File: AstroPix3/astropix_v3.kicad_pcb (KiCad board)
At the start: 4 copper layers, 51.3 x 48.9 mm, 50 parts, among them J1 pcie_GECCO, J10 SPI_right, J2 ChipRings, J3 TempSens, J4 SFOut, J5 sample_clock_out, J6 HV_in_external, J7 Conn_01x03, J9 SPI_left, U2 SN65LVDS4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

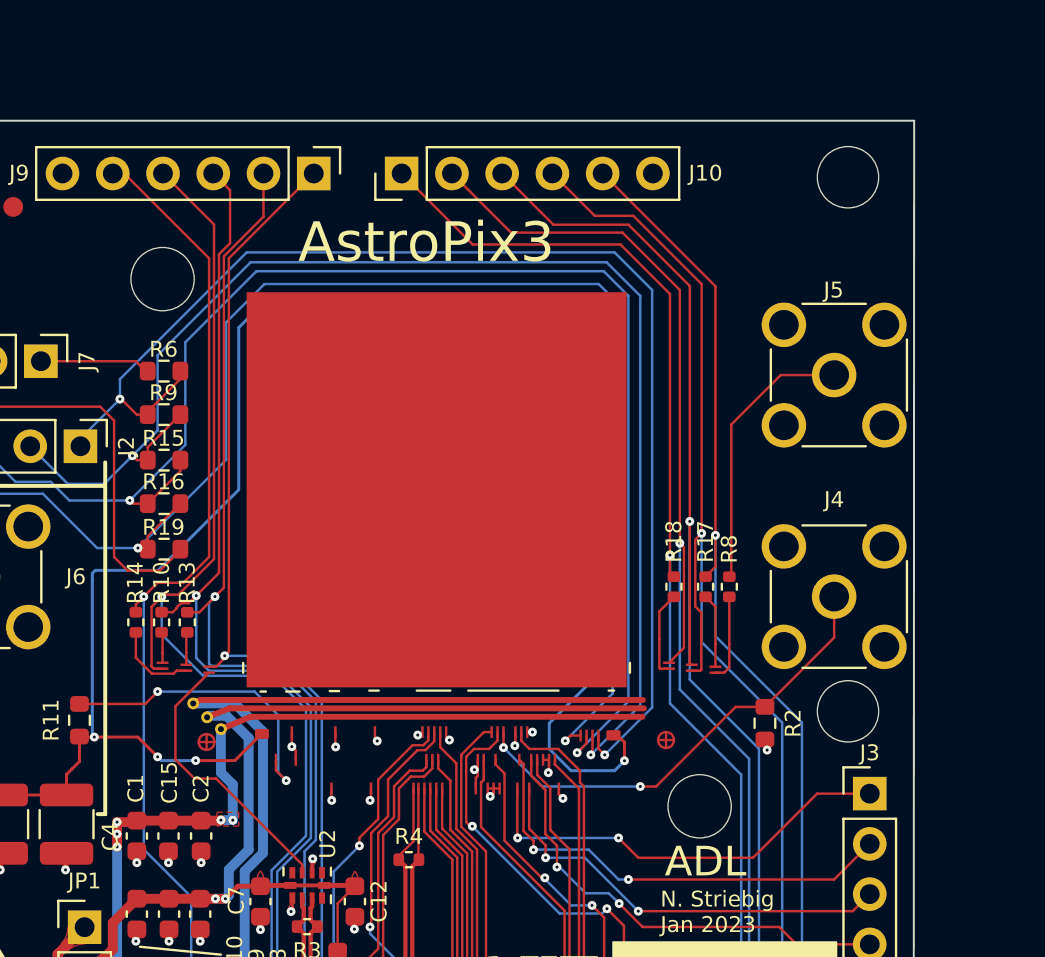
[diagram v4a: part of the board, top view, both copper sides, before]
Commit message: PCB: Connected HV Pad
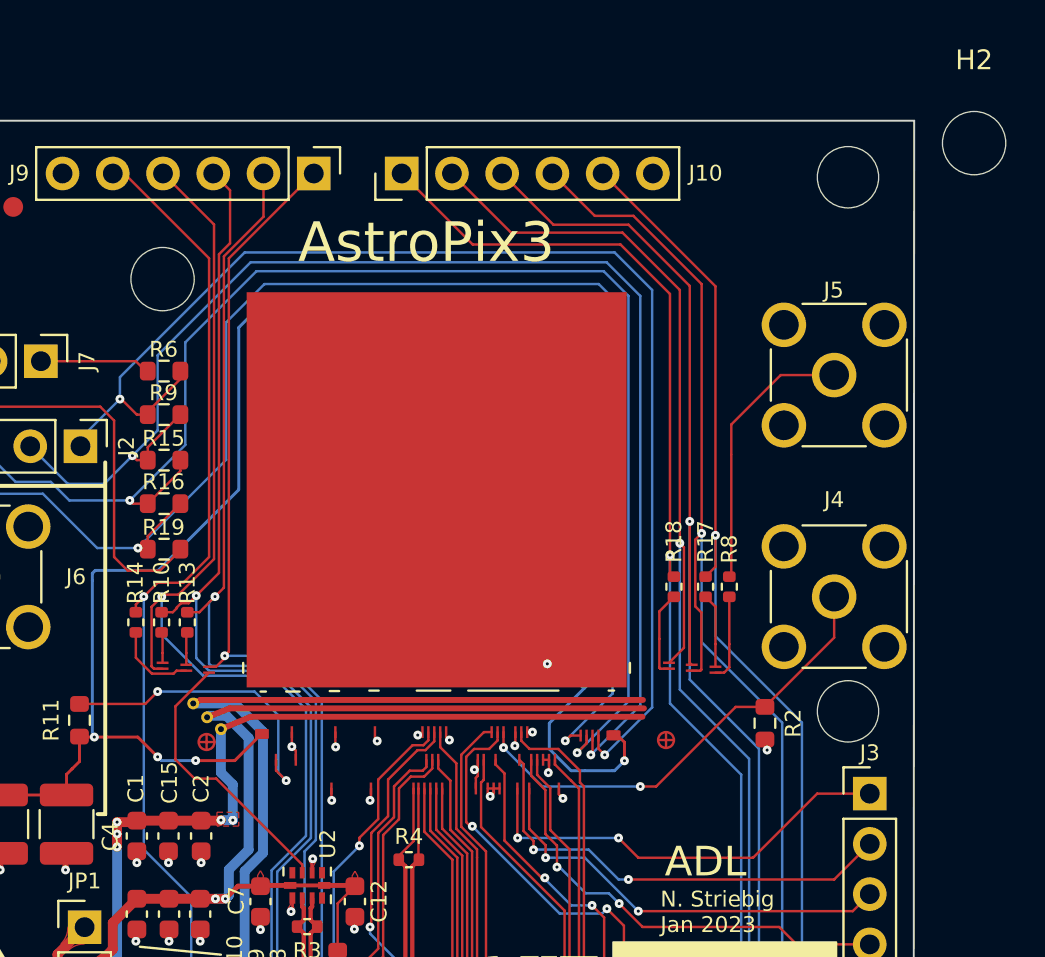
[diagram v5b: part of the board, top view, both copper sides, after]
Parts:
- moved H2 36.3 mm to (159.9, 53.1)
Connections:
- U5 pad B0: (no net) -> suba
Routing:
- net suba: track 95.3 -> 97.7 mm, vias 4 -> 5
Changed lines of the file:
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@@
   (net 9 "/res_n")
   (net 10 "Net-(J4-Pad1)")
-  (net 11 "Net-(R6-Pad1)")
+  (net 11 "Net-(J7-Pad1)")
   (net 12 "/DAC_blpix")
   (net 13 "/Inj")
@@
   (net 114 "/DAC_ThPMOS")
   (net 115 "Net-(R11-Pad2)")
-  (net 116 "Net-(R19-Pad2)")
+  (net 116 "Net-(J7-Pad3)")
   (footprint "Capacitor_SMD:C_0603_1608Metric" (layer "F.Cu")
     (at 120.7516 92.0496 -90)
@@
     (pad "" smd rect locked (at 12.885 -0.2) (size 0.07 0.2) (layers "Dwgs.User"))
     (pad "" smd rect locked (at 15.185 -0.2) (size 0.07 0.2) (layers "Dwgs.User"))
-    (pad "B0" smd rect locked (at 9.305 -9.8) (size 19.21 19.98) (layers "F.Cu" "F.Paste" "F.Mask"))
+    (pad "B0" smd rect locked (at 9.305 -9.8) (size 19.21 19.98) (layers "F.Cu" "F.Paste" "F.Mask")
+      (net 5 "suba") (pinfunction "sub!") (pintype "power_in"))
     (pad "B1" smd rect locked (at 0.325 2.54) (size 0.125 0.5) (layers "F.Cu" "F.Paste" "F.Mask")
       (net 5 "suba") (pinfunction "sub!") (pintype "power_in"))
@@
       (net 106 "/ring4") (pintype "passive"))
     (pad "2" smd roundrect (at 0.825 0) (size 0.8 0.95) (layers "F.Cu" "F.Paste" "F.Mask") (roundrect_rratio 0.25)
-      (net 116 "Net-(R19-Pad2)") (pintype "passive"))
+      (net 116 "Net-(J7-Pad3)") (pintype "passive"))
     (model "${KICAD6_3DMODEL_DIR}/Resistor_SMD.3dshapes/R_0603_1608Metric.wrl"
       (offset (xyz 0 0 0))
@@
     )
   )
+  (footprint "MountingHole:MountingHole_3.2mm_M3" (layer "F.Cu")
+    (at 159.875 53.075)
+    (descr "Mounting Hole 3.2mm, no annular, M3")
+    (tags "mounting hole 3.2mm no annular m3")
+    (property "Sheetfile" "astropix_v3.kicad_sch")
+    (property "Sheetname" "")
+    (attr exclude_from_pos_files)
+    (fp_text reference "H2" (at 0 -4.2) (layer "F.SilkS")
+      (effects (font (size 1 1) (thickness 0.15)))
+    )
+    (fp_text value "MountingHole" (at 0 4.2) (layer "F.Fab")
+      (effects (font (size 1 1) (thickness 0.15)))
+    )
+    (fp_text user "${REFERENCE}" (at 0 0) (layer "F.Fab")
+      (effects (font (size 1 1) (thickness 0.15)))
+    )
+    (fp_circle (center 0 0) (end 3.2 0) (layer "Cmts.User") (width 0.15) (fill none))
+    (fp_circle (center 0 0) (end 3.45 0) (layer "F.CrtYd") (width 0.05) (fill none))
+    (pad "" np_thru_hole circle (at 0 0) (size 3.2 3.2) (drill 3.2) (layers *.Cu *.Mask))
+  )
   (footprint "Resistor_SMD:R_0603_1608Metric" (layer "F.Cu")
     (at 127.7 94.725 -90)
@@
     (fp_line (start 0.8 0.4125) (end -0.8 0.4125) (layer "F.Fab") (width 0.1))
     (pad "1" smd roundrect (at -0.825 0) (size 0.8 0.95) (layers "F.Cu" "F.Paste" "F.Mask") (roundrect_rratio 0.25)
-      (net 11 "Net-(R6-Pad1)") (pintype "passive"))
+      (net 11 "Net-(J7-Pad1)") (pintype "passive"))
     (pad "2" smd roundrect (at 0.825 0) (size 0.8 0.95) (layers "F.Cu" "F.Paste" "F.Mask") (roundrect_rratio 0.25)
       (net 103 "/ring1") (pintype "passive"))
@@
     (fp_line (start -0.635 -1.27) (end 1.27 -1.27) (layer "F.Fab") (width 0.1))
     (pad "1" thru_hole rect (at 0 0 270) (size 1.7 1.7) (drill 1) (layers *.Cu *.Mask)
-      (net 11 "Net-(R6-Pad1)") (pinfunction "Pin_1") (pintype "passive"))
+      (net 11 "Net-(J7-Pad1)") (pinfunction "Pin_1") (pintype "passive"))
     (pad "2" thru_hole oval (at 0 2.54 270) (size 1.7 1.7) (drill 1) (layers *.Cu *.Mask)
       (net 23 "GND") (pinfunction "Pin_2") (pintype "passive"))
     (pad "3" thru_hole oval (at 0 5.08 270) (size 1.7 1.7) (drill 1) (layers *.Cu *.Mask)
-      (net 116 "Net-(R19-Pad2)") (pinfunction "Pin_3") (pintype "passive"))
+      (net 116 "Net-(J7-Pad3)") (pinfunction "Pin_3") (pintype "passive"))
     (model "${KICAD6_3DMODEL_DIR}/Connector_PinHeader_2.54mm.3dshapes/PinHeader_1x03_P2.54mm_Vertical.wrl"
       (offset (xyz 0 0 0))
@@
     )
   )
-  (footprint "MountingHole:MountingHole_3.2mm_M3" (layer "F.Cu")
-    (at 146 86.6)
-    (descr "Mounting Hole 3.2mm, no annular, M3")
-    (tags "mounting hole 3.2mm no annular m3")
-    (property "Sheetfile" "astropix_v3.kicad_sch")
-    (property "Sheetname" "")
-    (attr exclude_from_pos_files)
-    (fp_text reference "H2" (at 0 -4.2) (layer "F.SilkS") hide
-      (effects (font (size 0.8 0.8) (thickness 0.15)))
-    )
-    (fp_text value "MountingHole" (at 0 4.2) (layer "F.Fab") hide
-      (effects (font (size 1 1) (thickness 0.15)))
-    )
-    (fp_text user "${REFERENCE}" (at 0 0) (layer "F.Fab")
-      (effects (font (size 1 1) (thickness 0.15)))
-    )
-    (fp_circle (center 0 0) (end 3.2 0) (layer "Cmts.User") (width 0.15) (fill none))
-    (fp_circle (center 0 0) (end 3.45 0) (layer "F.CrtYd") (width 0.05) (fill none))
-    (pad "" np_thru_hole circle (at 0 0) (size 3.2 3.2) (drill 3.2) (layers *.Mask "F.Cu" "In1.Cu" "In2.Cu" "B.Cu"))
-  )
   (footprint "Connector_PinHeader_2.54mm:PinHeader_1x05_P2.54mm_Vertical" (layer "F.Cu")
     (at 154.6 85.96)
@@
   (via (at 120.525279 84.289388) (size 0.45) (drill 0.15) (layers "F.Cu" "B.Cu") (net 5))
   (via (at 115.4 83.1) (size 0.45) (drill 0.15) (layers "F.Cu" "B.Cu") (net 5))
+  (via (at 138.3 79.4) (size 0.45) (drill 0.15) (layers "F.Cu" "B.Cu") (net 5))
   (segment (start 122.7 62.4) (end 122.7 70.6) (width 0.15) (layer "B.Cu") (net 5))
+  (segment (start 138.3 79.4) (end 138.9 79.4) (width 0.15) (layer "B.Cu") (net 5))
   (segment (start 123.5 61.6) (end 122.7 62.4) (width 0.15) (layer "B.Cu") (net 5))
   (segment (start 122.7 70.6) (end 118.625 74.675) (width 0.15) (layer "B.Cu") (net 5))
@@
   (segment (start 118.789388 84.289388) (end 118.6 84.1) (width 0.15) (layer "B.Cu") (net 5))
   (segment (start 115.3 75.2) (end 115.3 83) (width 0.15) (layer "B.Cu") (net 5))
+  (segment (start 138.9 79.4) (end 140.15 80.65) (width 0.15) (layer "B.Cu") (net 5))
   (segment (start 141.6 84.8) (end 140.2 84.8) (width 0.15) (layer "B.Cu") (net 5))
   (segment (start 140.2 80.6) (end 140.8 80) (width 0.15) (layer "B.Cu") (net 5))
   (segment (start 140.2 84.8) (end 139.5 84.8) (width 0.15) (layer "B.Cu") (net 5))
-  (segment (start 138.4 82.4) (end 140.2 80.6) (width 0.15) (layer "B.Cu") (net 5))
+  (segment (start 140.15 80.65) (end 140.2 80.6) (width 0.15) (layer "B.Cu") (net 5))
   (segment (start 140.8 61.1) (end 124 61.1) (width 0.15) (layer "B.Cu") (net 5))
   (segment (start 140.8 80) (end 140.8 61.1) (width 0.15) (layer "B.Cu") (net 5))
@@
   (segment (start 120.525279 84.289388) (end 118.789388 84.289388) (width 0.15) (layer "B.Cu") (net 5))
   (segment (start 142.2 84.3) (end 141.7 84.8) (width 0.15) (layer "B.Cu") (net 5))
+  (segment (start 138.4 82.4) (end 140.15 80.65) (width 0.15) (layer "B.Cu") (net 5))
   (segment (start 141.7 84.8) (end 141.6 84.8) (width 0.15) (layer "B.Cu") (net 5))
   (segment (start 138.4 83.7) (end 138.4 82.4) (width 0.15) (layer "B.Cu") (net 5))
@@
   (via (at 141.2 84) (size 0.45) (drill 0.15) (layers "F.Cu" "B.Cu") (net 103))
   (via (at 116.694142 66.014314) (size 0.45) (drill 0.15) (layers "F.Cu" "B.Cu") (net 103))
-  (segment (start 123.1 58.6) (end 116.694142 65.005858) (width 0.125) (layer "B.Cu") (net 103))
+  (segment (start 116.694142 64.905858) (end 116.694142 66.014314) (width 0.125) (layer "B.Cu") (net 103))
   (segment (start 114.7 68.008456) (end 116.694142 66.014314) (width 0.125) (layer "B.Cu") (net 103))
-  (segment (start 114.7 68.4) (end 114.7 68.008456) (width 0.125) (layer "B.Cu") (net 103))
-  (segment (start 116.694142 65.005858) (end 116.694142 66.014314) (width 0.125) (layer "B.Cu") (net 103))
   (segment (start 143.6 60.5) (end 141.7 58.6) (width 0.125) (layer "B.Cu") (net 103))
-  (segment (start 141.7 58.6) (end 123.1 58.6) (width 0.125) (layer "B.Cu") (net 103))
+  (segment (start 141.7 58.6) (end 123 58.6) (width 0.125) (layer "B.Cu") (net 103))
   (segment (start 141.2 84) (end 143.6 81.6) (width 0.125) (layer "B.Cu") (net 103))
   (segment (start 143.6 81.6) (end 143.6 60.5) (width 0.125) (layer "B.Cu") (net 103))
+  (segment (start 114.7 68.4) (end 114.7 68.008456) (width 0.125) (layer "B.Cu") (net 103))
+  (segment (start 123 58.6) (end 116.694142 64.905858) (width 0.125) (layer "B.Cu") (net 103))
   (segment (start 140.585 83.915) (end 140.5 84) (width 0.125) (layer "F.Cu") (net 104))
   (segment (start 119.75 66.8) (end 118.1 68.45) (width 0.125) (layer "F.Cu") (net 104))

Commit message: PCB: V3 improvements
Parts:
- removed R1: 0, Resistor_SMD:R_1206_3216Metric
- moved H2 37.0 mm to (145.4, 87.1)
- moved R12 8.04 mm to (111.9, 82.3), turned to -90 degrees
- moved Logo2 0.50 mm to (109.1, 93.0)
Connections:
- J1 pad A1: -HV -> unconnected-(J1-PadA1)
- J1 pad B1: -HV -> unconnected-(J1-PadB1)
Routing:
- net /HV_in_ext: track 24.1 -> 7.46 mm
- net -HV: track 8.82 -> 0.00 mm, vias 1 -> 0
- net suba: track 97.7 -> 93.9 mm
- net /Inj: track 24.3 -> 24.9 mm
